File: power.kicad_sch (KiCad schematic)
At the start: 86 parts, among them Q1 PJE138K, Q2 PJE138K, Q3 SSM3J332R, Q4 PJE138K, Q5 SSM3J332R, Q6 PJE138K, Q7 SSM3J332R, U1 TLV70018_SC70, U4 TPS65150_HTSSOP, U5 MPQ7235GQBE, U6 TLV76701_WSON

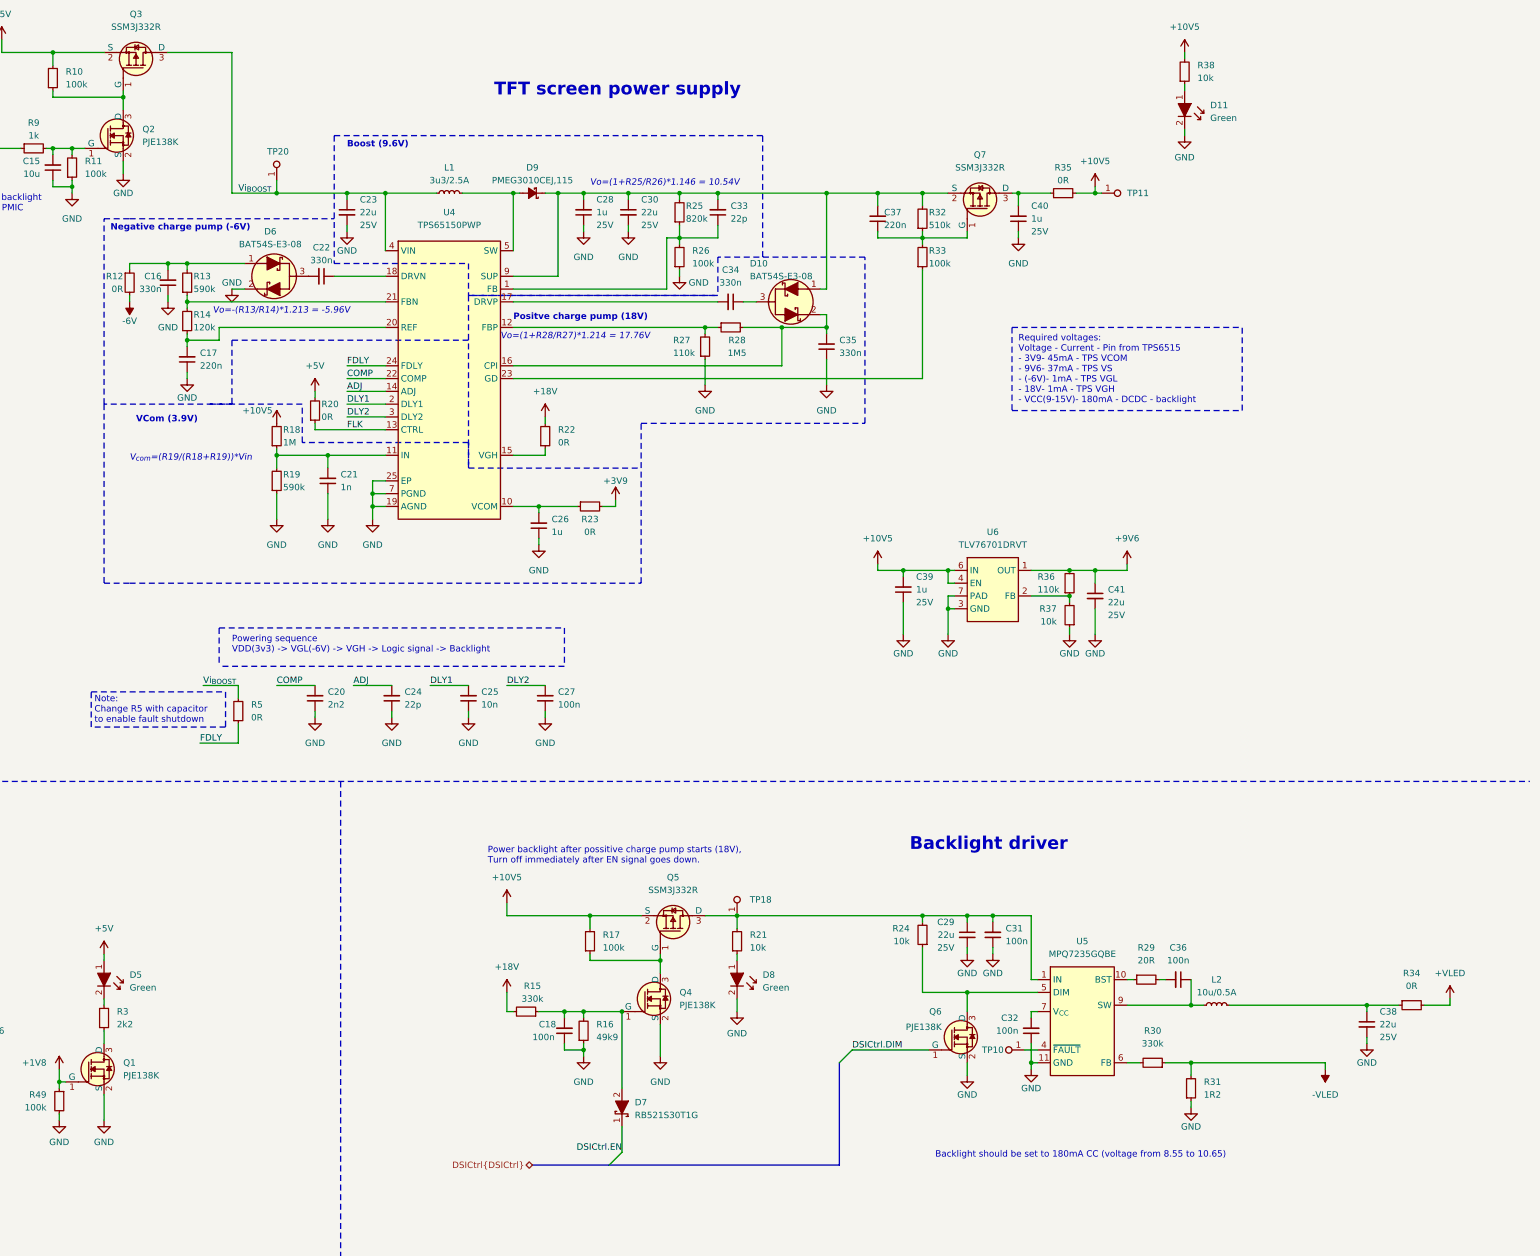
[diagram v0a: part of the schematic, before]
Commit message: [#58170] Clean ERC (update from lib; align to grid)
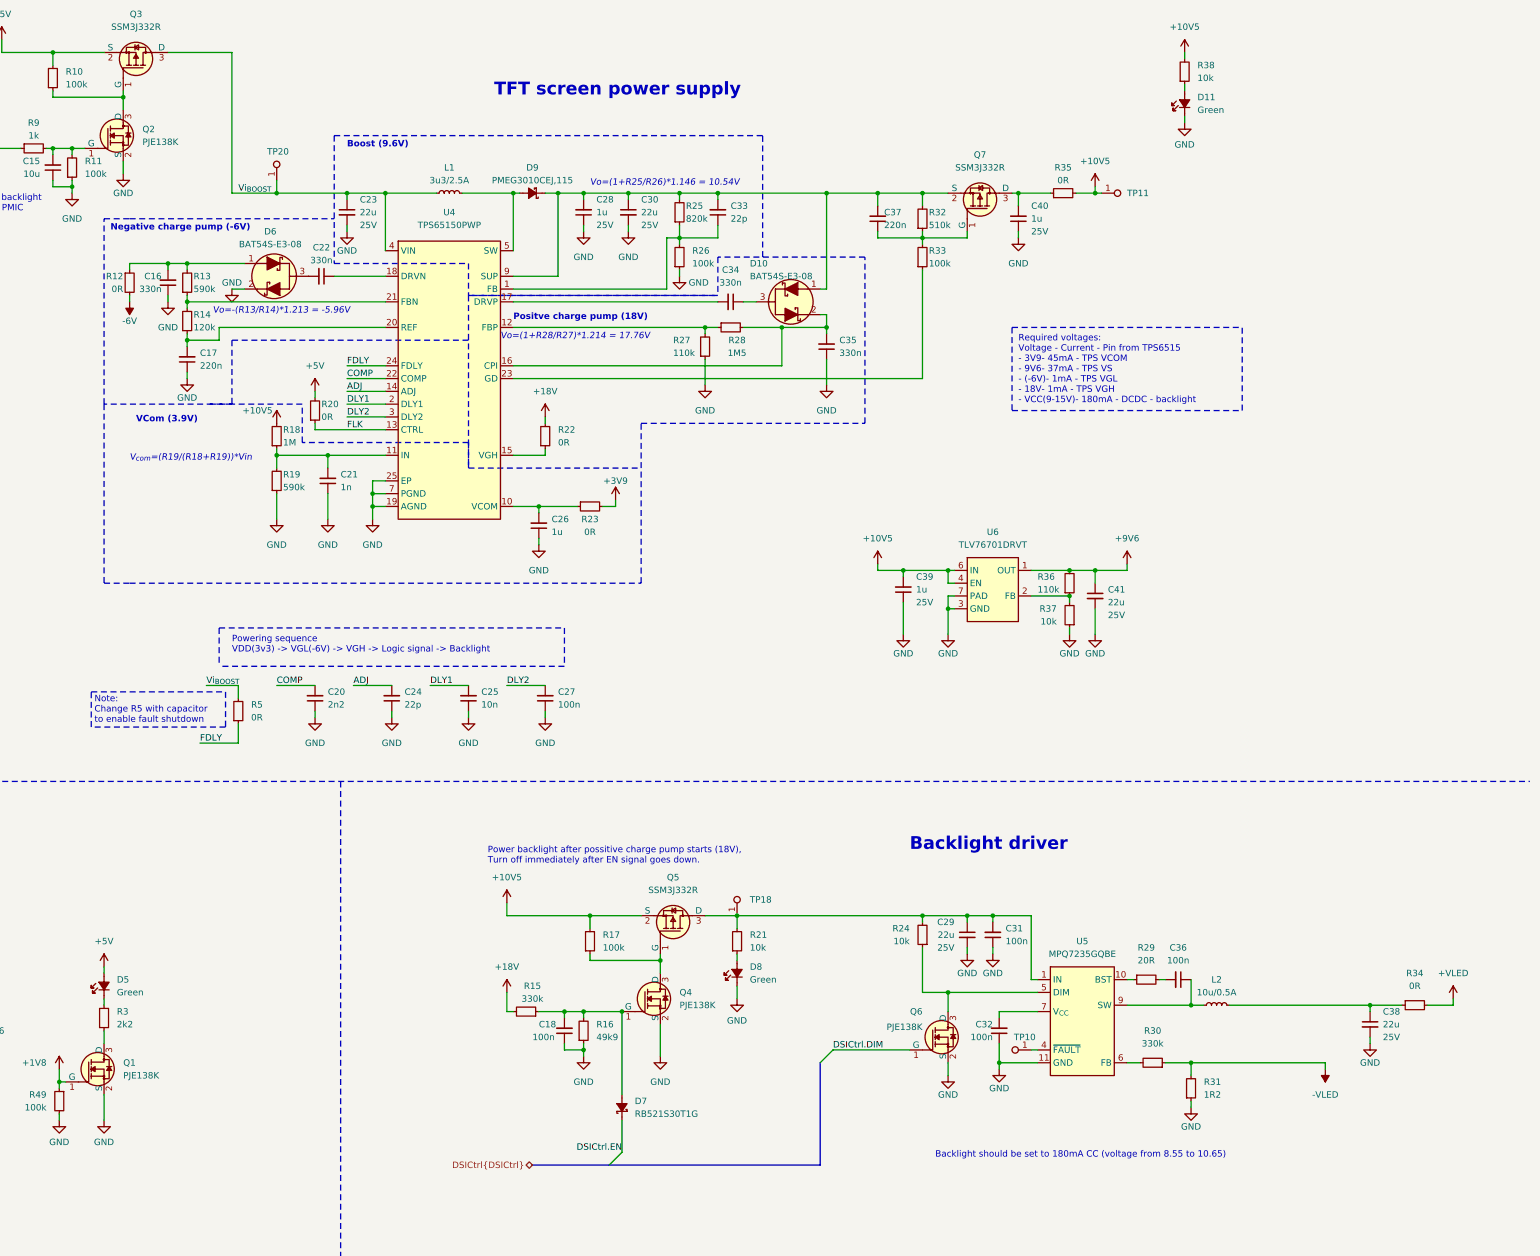
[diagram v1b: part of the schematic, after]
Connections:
- net +5V: now also D5.2 (A); no longer D5.1
- net GND: now also D11.1 (C), D8.1 (C); no longer D11.2, D8.2
- net at R38.1: now also D11.2 (A); no longer D11.1
- net at R3.2: now also D5.1 (C); no longer D5.2
- net at R21.1: now also D8.2 (A); no longer D8.1
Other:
- moved on the sheet: C32, C38, D7, Q6, R34, TP10

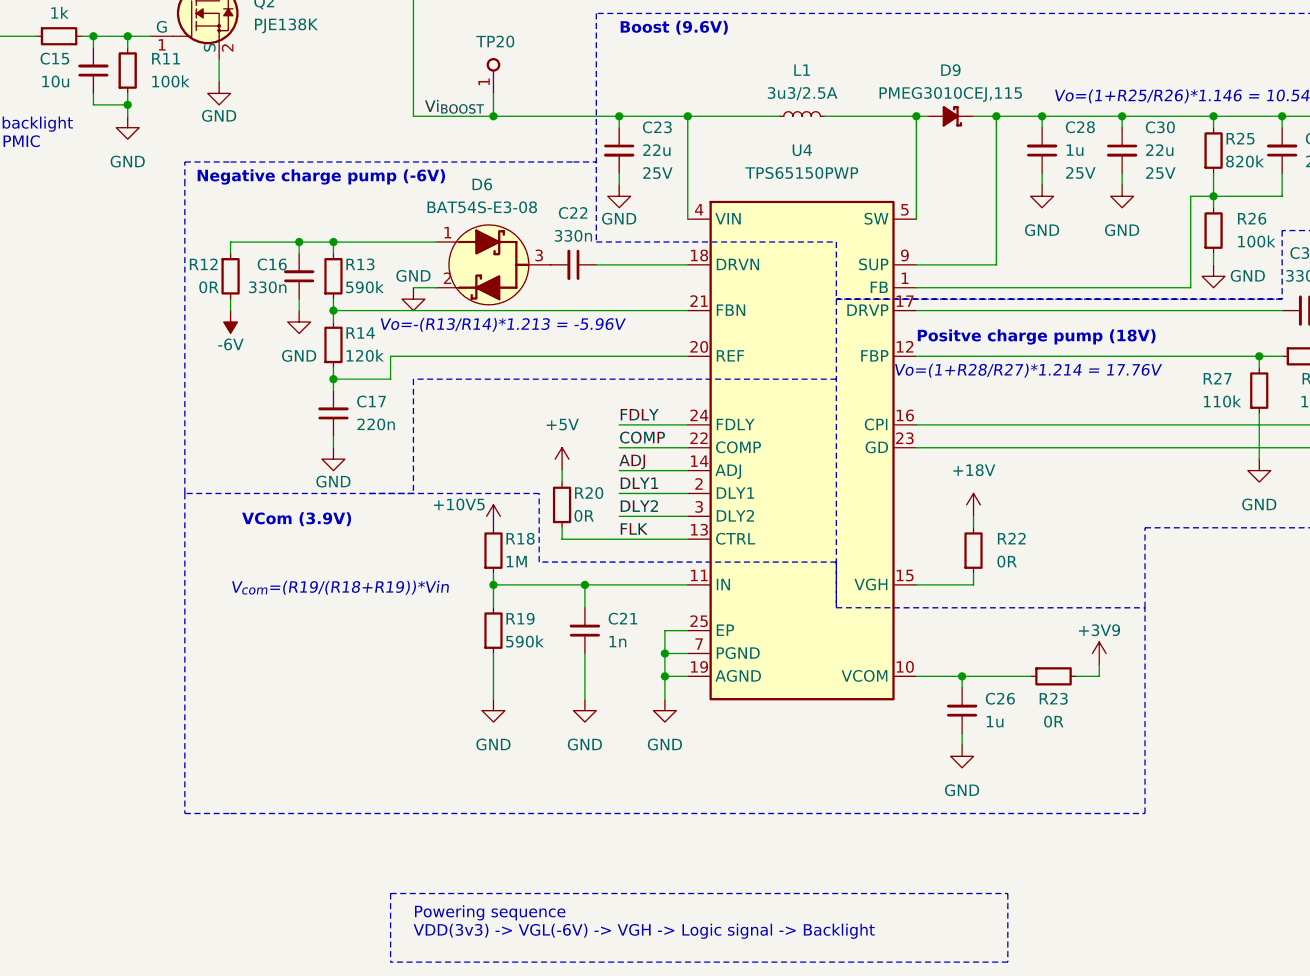
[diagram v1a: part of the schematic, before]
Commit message: [#58170] Add some testpoints
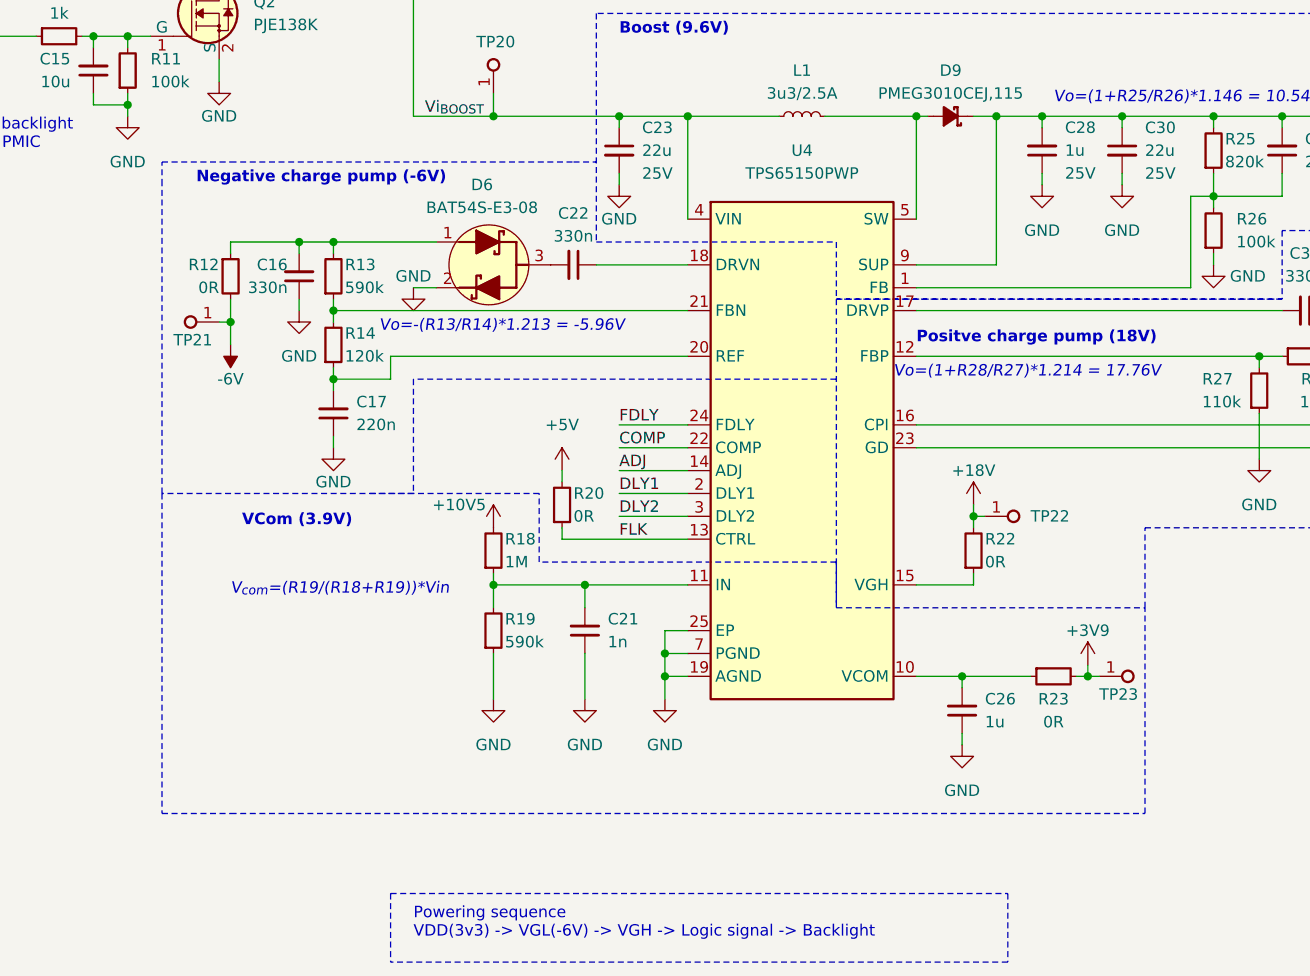
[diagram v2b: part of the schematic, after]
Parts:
- added TP21, TP22, TP23: TP_0.75mm_SMD, antmicro-footprints:TP_SMD_0.75mm, symbol antmicroTestPoints:TP_0.75mm_SMD
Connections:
- net +18V: now also TP22.1
- net +3V9: now also TP23.1
- net -6V: now also TP21.1

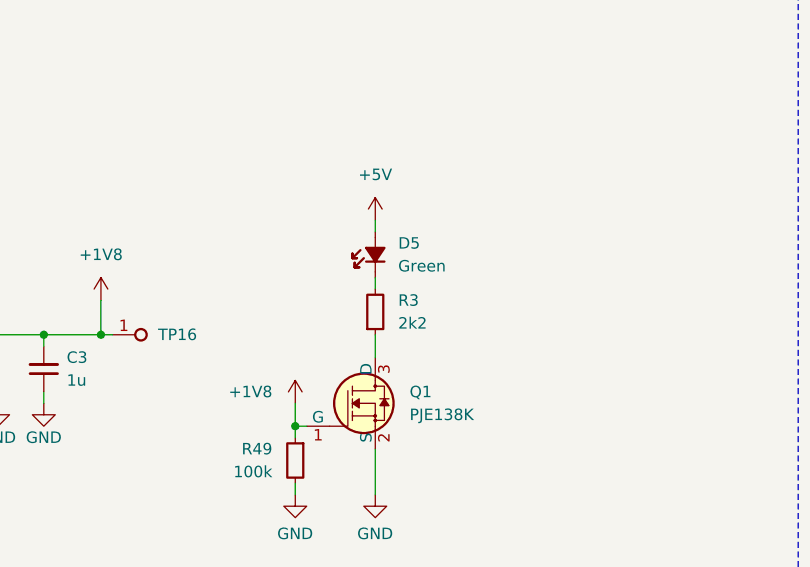
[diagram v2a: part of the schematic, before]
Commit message: [#58170] Add DNP pullups on I2C; Clean DRC
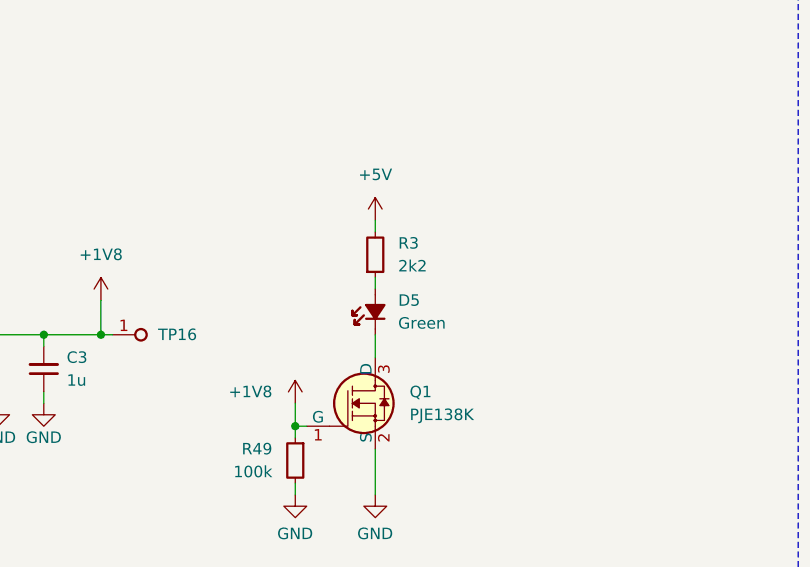
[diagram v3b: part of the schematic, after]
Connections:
- net +5V: now also R3.2; no longer D5.2 (A)
- net at R3.1: now also D5.2 (A); no longer Q1.3 (D)
- net at D5.1 (C): now also Q1.3 (D); no longer R3.2
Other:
- moved on the sheet: D5, R3
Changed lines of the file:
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@@
     )
   )
-  (symbol (lib_id "antmicroResistors0402:R_2k2_0402") (at 124.46 219.71 90) (unit 1)
-    (in_bom yes) (on_board yes) (dnp no) (fields_autoplaced)
-    (property "Reference" "R3" (at 127 215.9 90)
-      (effects (font (size 1.27 1.27)) (justify right))
-    )
-    (property "Value" "R_2k2_0402" (at 137.16 199.39 0)
-      (effects (font (size 1.27 1.27) (thickness 0.15)) (justify left bottom) hide)
-    )
-    (property "Footprint" "antmicro-footprints:R_0402_1005Metric" (at 139.7 199.39 0)
-      (effects (font (size 1.27 1.27) (thickness 0.15)) (justify left bottom) hide)
-    )
-    (property "Datasheet" "https://www.bourns.com/docs/product-datasheets/cr.pdf" (at 142.24 199.39 0)
-      (effects (font (size 1.27 1.27) (thickness 0.15)) (justify left bottom) hide)
-    )
-    (property "Manufacturer" "Bourns" (at 147.32 199.39 0)
-      (effects (font (size 1.27 1.27) (thickness 0.15)) (justify left bottom) hide)
-    )
-    (property "MPN" "CR0402-FX-2201GLF" (at 144.78 199.39 0)
-      (effects (font (size 1.27 1.27) (thickness 0.15)) (justify left bottom) hide)
-    )
-    (property "Val" "2k2" (at 127 218.44 90)
-      (effects (font (size 1.27 1.27) (thickness 0.15)) (justify right))
-    )
-    (property "License" "Apache-2.0" (at 149.86 199.39 0)
-      (effects (font (size 1.27 1.27) (thickness 0.15)) (justify left bottom) hide)
-    )
-    (property "Author" "Antmicro" (at 152.4 199.39 0)
-      (effects (font (size 1.27 1.27) (thickness 0.15)) (justify left bottom) hide)
-    )
-    (property "Tolerance" "1%" (at 134.62 199.39 0)
+  (symbol (lib_id "antmicroResistors0402:R_2k2_0402") (at 124.46 213.36 90) (unit 1)
+    (in_bom yes) (on_board yes) (dnp no) (fields_autoplaced)
+    (property "Reference" "R3" (at 127 209.55 90)
+      (effects (font (size 1.27 1.27)) (justify right))
+    )
+    (property "Value" "R_2k2_0402" (at 137.16 193.04 0)
+      (effects (font (size 1.27 1.27) (thickness 0.15)) (justify left bottom) hide)
+    )
+    (property "Footprint" "antmicro-footprints:R_0402_1005Metric" (at 139.7 193.04 0)
+      (effects (font (size 1.27 1.27) (thickness 0.15)) (justify left bottom) hide)
+    )
+    (property "Datasheet" "https://www.bourns.com/docs/product-datasheets/cr.pdf" (at 142.24 193.04 0)
+      (effects (font (size 1.27 1.27) (thickness 0.15)) (justify left bottom) hide)
+    )
+    (property "Manufacturer" "Bourns" (at 147.32 193.04 0)
+      (effects (font (size 1.27 1.27) (thickness 0.15)) (justify left bottom) hide)
+    )
+    (property "MPN" "CR0402-FX-2201GLF" (at 144.78 193.04 0)
+      (effects (font (size 1.27 1.27) (thickness 0.15)) (justify left bottom) hide)
+    )
+    (property "Val" "2k2" (at 127 212.09 90)
+      (effects (font (size 1.27 1.27) (thickness 0.15)) (justify right))
+    )
+    (property "License" "Apache-2.0" (at 149.86 193.04 0)
+      (effects (font (size 1.27 1.27) (thickness 0.15)) (justify left bottom) hide)
+    )
+    (property "Author" "Antmicro" (at 152.4 193.04 0)
+      (effects (font (size 1.27 1.27) (thickness 0.15)) (justify left bottom) hide)
+    )
+    (property "Tolerance" "1%" (at 134.62 193.04 0)
       (effects (font (size 1.27 1.27)) (justify left bottom) hide)
     )
@@
     )
   )
-  (symbol (lib_id "antmicroLEDIndicationDiscrete:LED_G_0603_598-8D80-107F") (at 124.46 213.36 90) (unit 1)
-    (in_bom yes) (on_board yes) (dnp no) (fields_autoplaced)
-    (property "Reference" "D5" (at 127 209.55 90)
-      (effects (font (size 1.27 1.27) (thickness 0.15)) (justify right))
-    )
-    (property "Value" "LED_G_0603_598-8D80-107F" (at 132.08 190.5 0)
-      (effects (font (size 1.27 1.27) (thickness 0.15)) (justify left bottom) hide)
-    )
-    (property "Footprint" "antmicro-footprints:LED_0603_1608Metric_G" (at 134.62 190.5 0)
-      (effects (font (size 1.27 1.27) (thickness 0.15)) (justify left bottom) hide)
-    )
-    (property "Datasheet" "https://www.dialight.com/wp-content/uploads/2021/07/DIA_Selector_Guide_SMD_042321.pdf" (at 137.16 190.5 0)
-      (effects (font (size 1.27 1.27) (thickness 0.15)) (justify left bottom) hide)
-    )
-    (property "MPN" "598-8D80-107F" (at 139.7 190.5 0)
-      (effects (font (size 1.27 1.27) (thickness 0.15)) (justify left bottom) hide)
-    )
-    (property "Manufacturer" "Dialight" (at 142.24 190.5 0)
-      (effects (font (size 1.27 1.27) (thickness 0.15)) (justify left bottom) hide)
-    )
-    (property "Author" "Antmicro" (at 144.78 190.5 0)
-      (effects (font (size 1.27 1.27) (thickness 0.15)) (justify left bottom) hide)
-    )
-    (property "License" "Apache-2.0" (at 147.32 190.5 0)
-      (effects (font (size 1.27 1.27) (thickness 0.15)) (justify left bottom) hide)
-    )
-    (property "Color" "Green" (at 127 212.09 90)
-      (effects (font (size 1.27 1.27)) (justify right))
-    )
+  (symbol (lib_id "antmicroLEDIndicationDiscrete:LED_G_0603_598-8D80-107F") (at 124.46 219.71 90) (unit 1)
+    (in_bom yes) (on_board yes) (dnp no) (fields_autoplaced)
+    (property "Reference" "D5" (at 127 215.9 90)
+      (effects (font (size 1.27 1.27) (thickness 0.15)) (justify right))
+    )
+    (property "Value" "LED_G_0603_598-8D80-107F" (at 132.08 196.85 0)
+      (effects (font (size 1.27 1.27) (thickness 0.15)) (justify left bottom) hide)
+    )
+    (property "Footprint" "antmicro-footprints:LED_0603_1608Metric_G" (at 134.62 196.85 0)
+      (effects (font (size 1.27 1.27) (thickness 0.15)) (justify left bottom) hide)
+    )
+    (property "Datasheet" "https://www.dialight.com/wp-content/uploads/2021/07/DIA_Selector_Guide_SMD_042321.pdf" (at 137.16 196.85 0)
+      (effects (font (size 1.27 1.27) (thickness 0.15)) (justify left bottom) hide)
+    )
+    (property "MPN" "598-8D80-107F" (at 139.7 196.85 0)
+      (effects (font (size 1.27 1.27) (thickness 0.15)) (justify left bottom) hide)
+    )
+    (property "Manufacturer" "Dialight" (at 142.24 196.85 0)
+      (effects (font (size 1.27 1.27) (thickness 0.15)) (justify left bottom) hide)
+    )
+    (property "Author" "Antmicro" (at 144.78 196.85 0)
+      (effects (font (size 1.27 1.27) (thickness 0.15)) (justify left bottom) hide)
+    )
+    (property "License" "Apache-2.0" (at 147.32 196.85 0)
+      (effects (font (size 1.27 1.27) (thickness 0.15)) (justify left bottom) hide)
+    )
+    (property "Color" "Green" (at 127 218.44 90)
+      (effects (font (size 1.27 1.27)) (justify right))
+    )
